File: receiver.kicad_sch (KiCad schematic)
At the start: 126 parts, among them U1 AD8334ACPZ, U4 AD8334ACPZ, U8 TLV9354IDR, U9 TLV9354IDR

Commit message: DONE (inshallah)
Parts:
- removed C49, C51, C53, C55, C58, C59, C64, C65: 100nF 0805, symbol Device:C
- removed C50, C52, C54, C56, C61, C62, C70, C71: 1nF 0805, symbol Device:C
- removed JP10, JP13, JP14, JP15, JP16, JP6, JP8, JP9: SolderJumper_2_Open, symbol Jumper:SolderJumper_2_Open
- added R120, R121, R122, R123, R124, R125, R126, R127: 90R 0805, symbol Device:R
- added TP17, TP18, TP19, TP20, TP21, TP22, TP23, TP24, TP25, TP26, TP27, TP28, TP29, TP30, TP31, TP32, TP33, TP34, TP35, TP36, TP37, TP38, TP39, TP40, TP41, TP42, TP43, TP44, TP45, TP46, TP47, TP48, TP49, TP50, TP51, TP52: RCT-0C, digikey-footprints:PROBE_PAD_0805, symbol dk_Test-Points:RCT-0C
- R41: value 90R 0806 -> 90R 0805
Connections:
- net ADC1: now also R120.2; no longer R53.2, U8.1 (OUT_A)
- net ADC1_H: now also TP29.1
- net ADC1_L: now also TP33.1
- net ADC2: now also R123.2; no longer R58.1, U8.7 (OUT_B)
- net ADC2_H: now also TP30.1
- net ADC2_L: now also TP34.1
- net ADC3: now also R122.1; no longer R66.1, U8.8 (OUT_C)
- net ADC3_H: now also TP31.1
- net ADC3_L: now also TP35.1
- net ADC4: now also R121.1; no longer R65.2, U8.14 (OUT_D)
- net ADC4_H: now also TP32.1
- net ADC4_L: now also TP36.1
- net ADC5: now also R124.2; no longer R73.2, U9.1 (OUT_A)
- net ADC5_H: now also TP37.1
- net ADC5_L: now also TP41.1
- net ADC6: now also R126.2; no longer R74.1, U9.7 (OUT_B)
- net ADC6_H: now also TP38.1
- net ADC6_L: now also TP42.1
- net ADC7: now also R127.1; no longer R75.1, U9.8 (OUT_C)
- net ADC7_H: now also TP39.1
- net ADC7_L: now also TP43.1
- net ADC8: now also R125.1; no longer R76.2, U9.14 (OUT_D)
- net ADC8_H: now also TP40.1
- net ADC8_L: now also TP44.1
- net GAIN12_A: now also TP17.1
- net GAIN12_B: now also TP19.1
- net GAIN34_A: now also TP18.1
- net GAIN34_B: now also TP20.1
- net LNAA1_N: now also TP45.1
- net LNAA2_N: now also TP46.1
- net LNAA3_N: now also TP47.1
- net LNAA4_N: now also TP48.1
- net LNAA5_N: now also TP49.1
- net LNAA6_N: now also TP50.1
- net LNAA7_N: now also TP51.1
- net LNAA8_N: now also TP52.1
- new net: R127.2, R75.1, TP28.1, U9.8 (OUT_C)
- new net: R124.1, R73.2, TP25.1, U9.1 (OUT_A)
- new net: R125.2, R76.2, TP26.1, U9.14 (OUT_D)
- new net: R126.1, R74.1, TP27.1, U9.7 (OUT_B)
- new net: R121.2, R65.2, TP22.1, U8.14 (OUT_D)
- new net: R123.1, R58.1, TP23.1, U8.7 (OUT_B)
- new net: R120.1, R53.2, TP21.1, U8.1 (OUT_A)
- new net: R122.2, R66.1, TP24.1, U8.8 (OUT_C)
- no-connect marks 0 -> 8
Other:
- moved on the sheet: C47, C48, C67, C68, L1, L2, L3, L4, R38, R39, R40, R41

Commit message: started layout, 20-30% done
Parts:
- C31, C32, C33, C34, C35, C36, C37, C38, C39, C40, C41, C42, C43, C44, C45, C46, C47, C48, C57, C60, C63, C66, C67, C68, C69, C72, C73, C74, C75, C76, C77, C78, C79, C80, C81, C82, C83, C84: footprint (none) -> Capacitor_SMD:C_0603_1608Metric
- JP11, JP12, JP4, JP5: footprint (none) -> Jumper:SolderJumper-3_P1.3mm_Open_Pad1.0x1.5mm
- L1, L2, L3, L4: footprint (none) -> Inductor_SMD:L_0805_2012Metric
- R100, R103, R104, R120, R121, R122, R123, R124, R125, R126, R127, R32, R33, R34, R35, R36, R37, R38, R39, R40, R41, R42, R43, R44, R45, R46, R47, R51, R52, R53, R54, R55, R56, R57, R58, R59, R60, R61, R62, R63, R64, R65, R66, R67, R68, R69, R70, R71, R72, R73, R74, R75, R76, R77, R78, R79, R80, R81, R82, R99: footprint (none) -> Resistor_SMD:R_0603_1608Metric
- U8, U9: footprint SOIC_9354IDR_TEX -> TLV9354IDR:SOIC_9354IDR_TEX

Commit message: fininshed 90% placement, only power section needs refinement, next sprint the stackup will be decided, probably 6 layers
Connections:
- net TR_OUT1: now also C36.1, R34.1, U4.1 (INH2); no longer C35.1, R35.1, U4.62 (INH1)
- net TR_OUT2: now also C37.1, R33.1, U4.16 (INH3); no longer C36.1, R34.1, U4.1 (INH2)
- net TR_OUT3: now also C38.1, R32.1, U4.19 (INH4); no longer C37.1, R33.1, U4.16 (INH3)
- net TR_OUT4: now also C35.1, R35.1, U4.62 (INH1); no longer C38.1, R32.1, U4.19 (INH4)
- net TR_OUT5: now also C60.1, R46.1, U1.1 (INH2); no longer C57.1, R47.1, U1.62 (INH1)
- net TR_OUT6: now also C63.1, R45.1, U1.16 (INH3); no longer C60.1, R46.1, U1.1 (INH2)
- net TR_OUT7: now also C66.1, R44.1, U1.19 (INH4); no longer C63.1, R45.1, U1.16 (INH3)
- net TR_OUT8: now also C57.1, R47.1, U1.62 (INH1); no longer C66.1, R44.1, U1.19 (INH4)
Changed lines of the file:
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@@
 	)
 	(label "TR_OUT7"
-		(at 306.07 72.39 180)
+		(at 306.07 74.93 180)
 		(effects
 			(font
@@
 	)
 	(label "TR_OUT6"
-		(at 306.07 69.85 180)
+		(at 306.07 72.39 180)
 		(effects
 			(font
@@
 	)
 	(label "TR_OUT5"
-		(at 306.07 67.31 180)
+		(at 306.07 69.85 180)
 		(effects
 			(font
@@
 	)
 	(label "TR_OUT1"
-		(at 104.14 66.04 180)
+		(at 104.14 68.58 180)
 		(effects
 			(font
@@
 	)
 	(label "TR_OUT3"
-		(at 104.14 71.12 180)
+		(at 104.14 73.66 180)
 		(effects
 			(font
@@
 	)
 	(label "TR_OUT8"
-		(at 306.07 74.93 180)
+		(at 306.07 67.31 180)
 		(effects
 			(font
@@
 	)
 	(label "TR_OUT4"
-		(at 104.14 73.66 180)
+		(at 104.14 66.04 180)
 		(effects
 			(font
@@
 	)
 	(label "TR_OUT2"
-		(at 104.14 68.58 180)
+		(at 104.14 71.12 180)
 		(effects
 			(font
@@
 	(hierarchical_label "TR_OUT2"
 		(shape input)
-		(at 24.13 68.58 180)
+		(at 24.13 71.12 180)
 		(effects
 			(font
@@
 	(hierarchical_label "TR_OUT8"
 		(shape input)
+		(at 226.06 67.31 180)
+		(effects
+			(font
+				(size 1.27 1.27)
+			)
+			(justify right)
+		)
+	)
+	(hierarchical_label "TR_OUT5"
+		(shape input)
+		(at 226.06 69.85 180)
+		(effects
+			(font
+				(size 1.27 1.27)
+			)
+			(justify right)
+		)
+	)
+	(hierarchical_label "TR_OUT7"
+		(shape input)
 		(at 226.06 74.93 180)
-		(effects
-			(font
-				(size 1.27 1.27)
-			)
-			(justify right)
-		)
-	)
-	(hierarchical_label "TR_OUT5"
-		(shape input)
-		(at 226.06 67.31 180)
-		(effects
-			(font
-				(size 1.27 1.27)
-			)
-			(justify right)
-		)
-	)
-	(hierarchical_label "TR_OUT7"
-		(shape input)
-		(at 226.06 72.39 180)
 		(effects
 			(font
@@
 	(hierarchical_label "TR_OUT1"
 		(shape input)
-		(at 24.13 66.04 180)
+		(at 24.13 68.58 180)
 		(effects
 			(font
@@
 	(hierarchical_label "TR_OUT6"
 		(shape input)
-		(at 226.06 69.85 180)
+		(at 226.06 72.39 180)
 		(effects
 			(font
@@
 	(hierarchical_label "TR_OUT3"
 		(shape input)
-		(at 24.13 71.12 180)
+		(at 24.13 73.66 180)
 		(effects
 			(font
@@
 	(hierarchical_label "TR_OUT4"
 		(shape input)
-		(at 24.13 73.66 180)
-		(effects
-			(font
+		(at 24.13 66.04 180)
+		(effects
+			(font

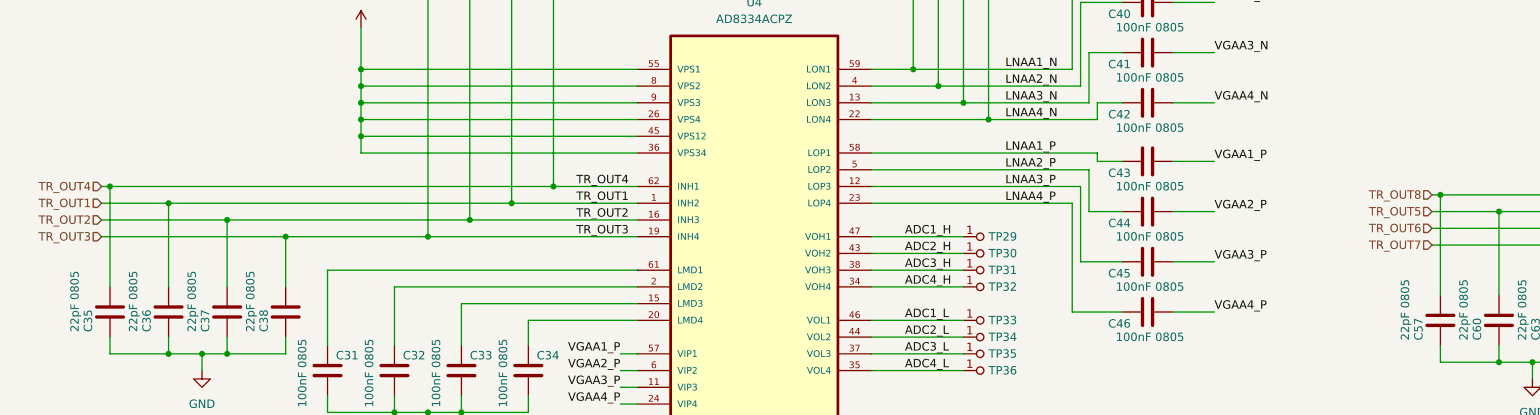
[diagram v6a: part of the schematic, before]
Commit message: finished power section, 70% AFE, re-think the stackup and the AFE stage near the MCU
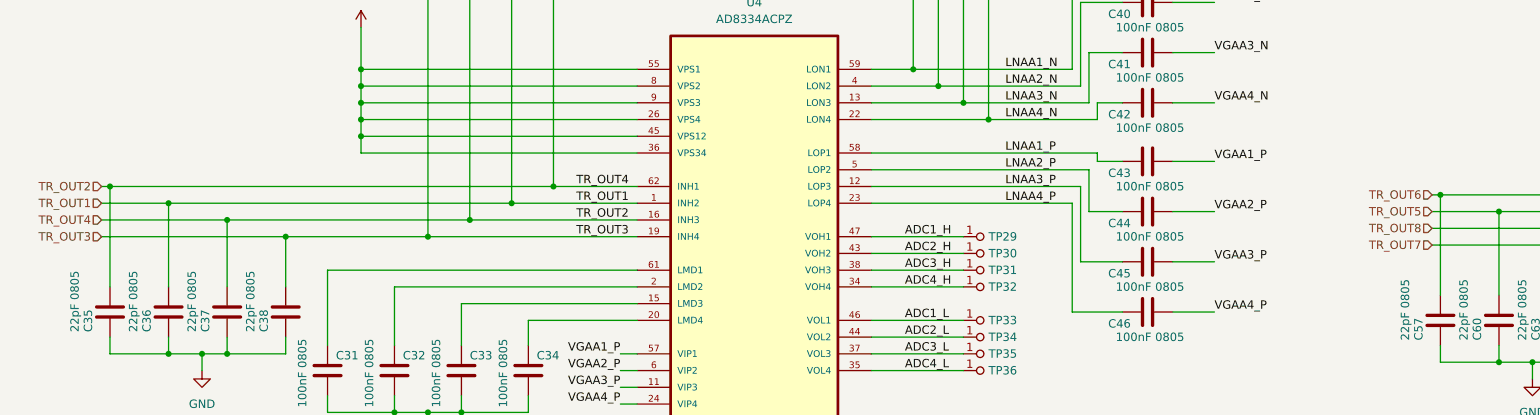
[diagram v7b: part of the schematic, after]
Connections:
- net TR_OUT4 is gone; now on net TR_OUT2: C35.1, R35.1, U4.62 (INH1)
- net TR_OUT8 is gone; now on net TR_OUT6: C57.1, R47.1, U1.62 (INH1)
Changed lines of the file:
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@@
 	(hierarchical_label "TR_OUT2"
 		(shape input)
-		(at 24.13 71.12 180)
+		(at 24.13 66.04 180)
 		(effects
 			(font
@@
 	(hierarchical_label "TR_OUT8"
 		(shape input)
-		(at 226.06 67.31 180)
+		(at 226.06 72.39 180)
 		(effects
 			(font
@@
 	(hierarchical_label "TR_OUT6"
 		(shape input)
-		(at 226.06 72.39 180)
+		(at 226.06 67.31 180)
 		(effects
 			(font
@@
 	(hierarchical_label "TR_OUT4"
 		(shape input)
-		(at 24.13 66.04 180)
+		(at 24.13 71.12 180)
 		(effects
 			(font

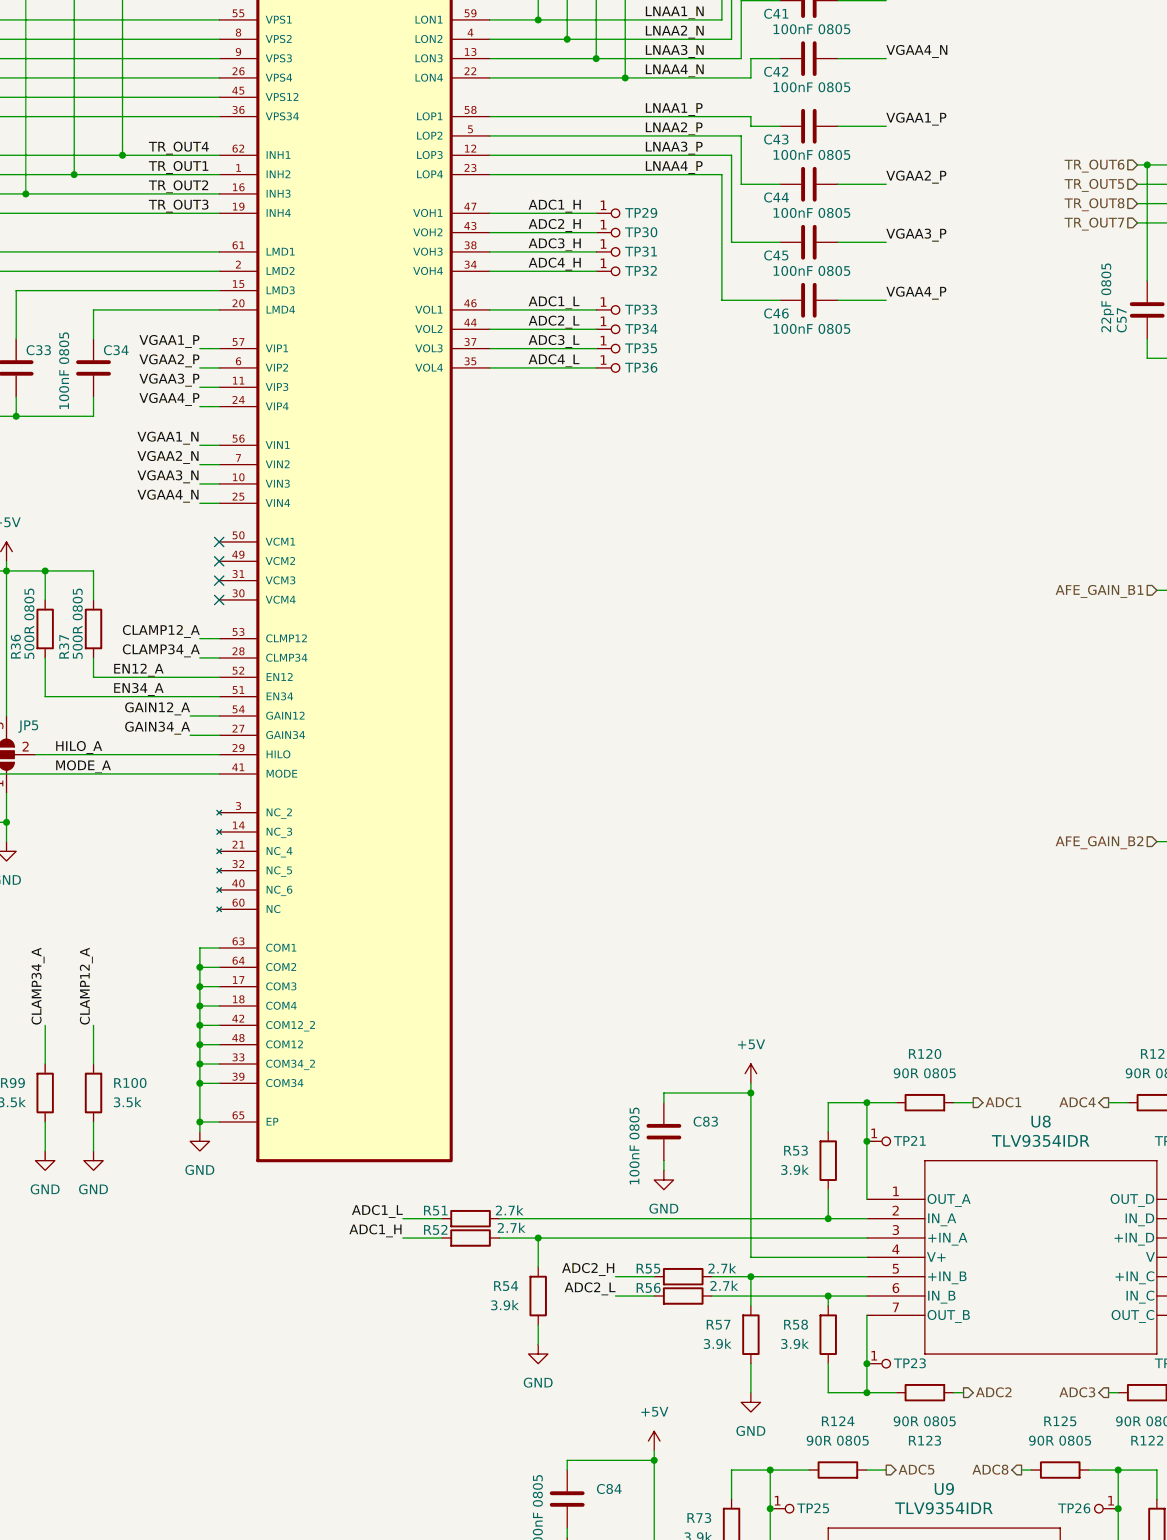
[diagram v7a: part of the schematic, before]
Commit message: Finished 70% fr this time, power planes are remaining and some minor connections to the AFE's power & cfg pins, dont forget xrst
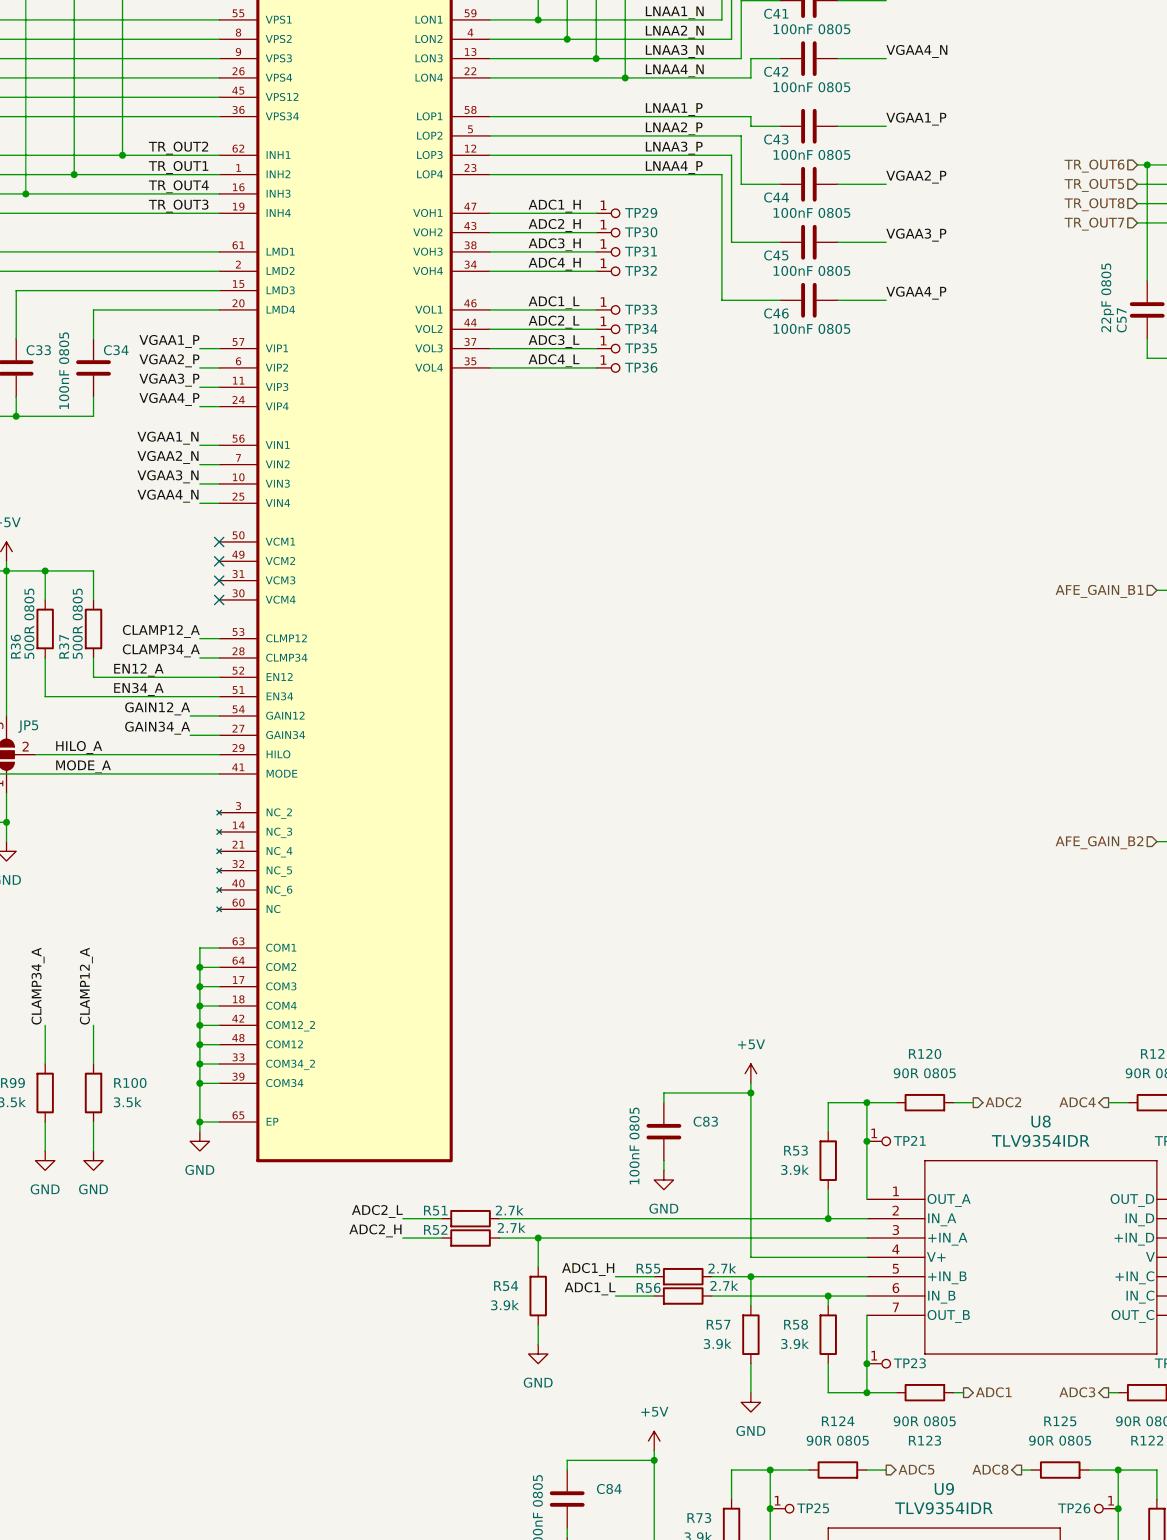
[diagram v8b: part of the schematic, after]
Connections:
- net ADC1: now also R123.2; no longer R120.2
- net ADC1_H: now also R55.2; no longer R52.2
- net ADC1_L: now also R56.2; no longer R51.2
- net ADC2: now also R120.2; no longer R123.2
- net ADC2_H: now also R52.2; no longer R55.2
- net ADC2_L: now also R51.2; no longer R56.2
- net TR_OUT2: no longer C37.1, R33.1, U4.16 (INH3)
- new net TR_OUT4: C37.1, R33.1, U4.16 (INH3)
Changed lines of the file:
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@@
+		)
+	)
+	(label "ADC2_L"
+		(at 129.54 205.74 180)
+		(effects
+			(font
+				(size 1.27 1.27)
+			)
+			(justify right bottom)
 		)
 	)
@@
 		)
 	)
-	(label "ADC1_L"
-		(at 129.54 205.74 180)
+	(label "ADC2_H"
+		(at 129.54 208.28 180)
 		(effects
 			(font
@@
 		)
 	)
+	(label "ADC1_L"
+		(at 157.48 215.9 180)
+		(effects
+			(font
+				(size 1.27 1.27)
+			)
+			(justify right bottom)
+		)
+	)
 	(label "ADC3_L"
 		(at 269.24 215.9 0)
@@
 		)
 	)
-	(label "ADC2_H"
-		(at 157.48 213.36 180)
-		(effects
-			(font
-				(size 1.27 1.27)
-			)
-			(justify right bottom)
-		)
-	)
 	(label "GAIN12_A"
 		(at 101.6 139.7 180)
@@
 		)
 	)
-	(label "ADC1_H"
-		(at 129.54 208.28 180)
-		(effects
-			(font
-				(size 1.27 1.27)
-			)
-			(justify right bottom)
-		)
-	)
 	(label "ADC3_H"
 		(at 269.24 213.36 0)
@@
 		)
 	)
+	(label "ADC1_H"
+		(at 157.48 213.36 180)
+		(effects
+			(font
+				(size 1.27 1.27)
+			)
+			(justify right bottom)
+		)
+	)
 	(label "ADC8_L"
 		(at 284.48 254 0)
@@
 		)
 	)
-	(label "ADC2_L"
-		(at 157.48 215.9 180)
-		(effects
-			(font
-				(size 1.27 1.27)
-			)
-			(justify right bottom)
-		)
-	)
 	(label "LNAA4_P"
 		(at 161.29 68.58 0)
@@
 	)
 	(label "TR_OUT4"
-		(at 104.14 66.04 180)
+		(at 104.14 71.12 180)
 		(effects
 			(font
@@
 	)
 	(label "TR_OUT2"
-		(at 104.14 71.12 180)
+		(at 104.14 66.04 180)
 		(effects
 			(font
@@
 	(hierarchical_label "ADC2"
 		(shape output)
-		(at 203.2 228.6 0)
+		(at 204.47 190.5 0)
 		(effects
 			(font
@@
 	(hierarchical_label "ADC1"
 		(shape output)
-		(at 204.47 190.5 0)
-		(effects
-			(font
+		(at 203.2 228.6 0)
+		(effects
+			(font
